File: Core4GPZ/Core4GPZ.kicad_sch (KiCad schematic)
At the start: 5 parts, among them J1 Delphi_Sicma_24, J2 Delphi_Sicma_24, U1 core4, U2 MPX4250

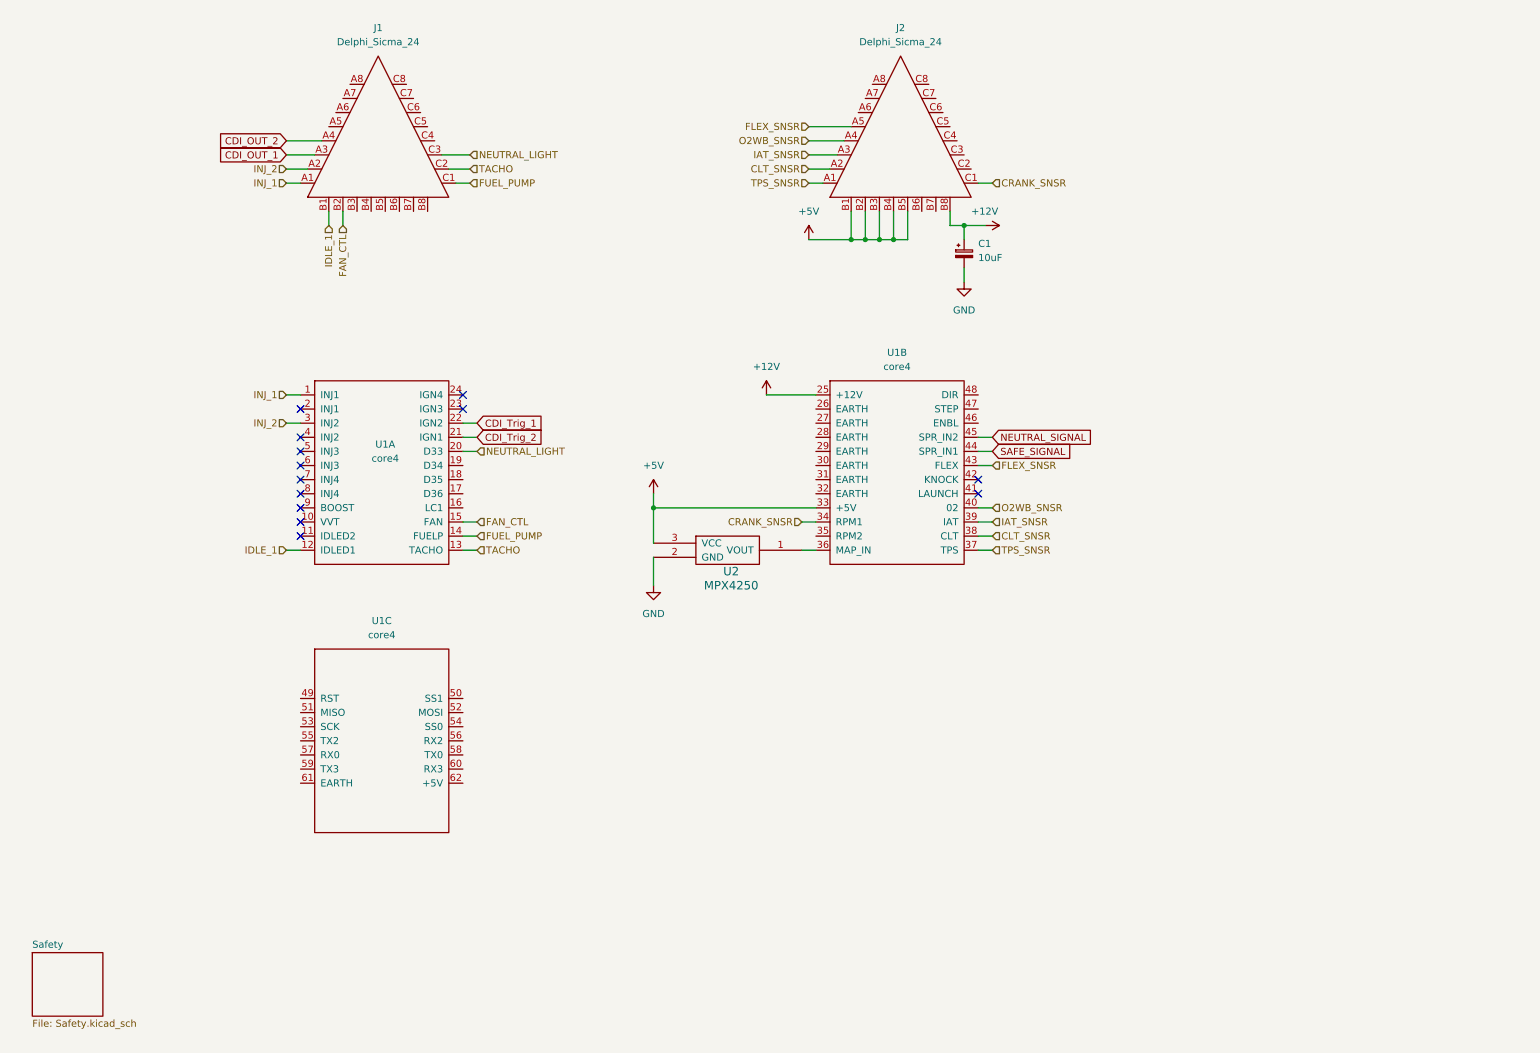
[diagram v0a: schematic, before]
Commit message: Add a splited CDI module. First Design of Ignition coil driver
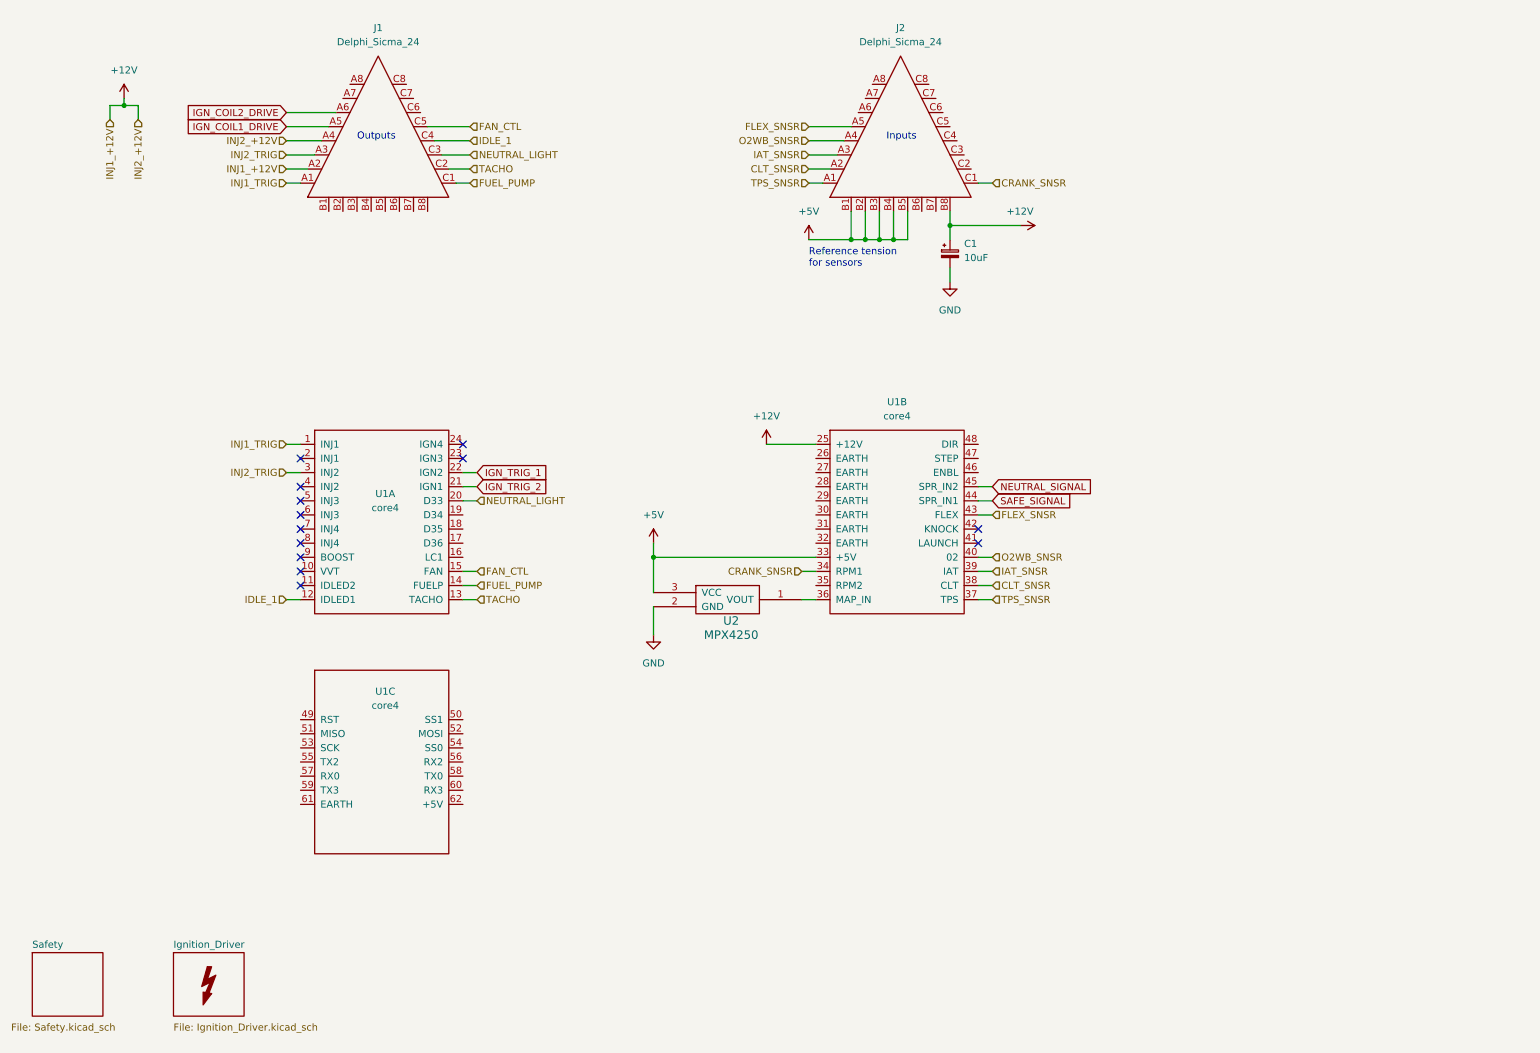
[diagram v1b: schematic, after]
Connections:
- net CDI_OUT_2 is gone; now on net +12V: J1.A4
- net +12V: now also J1.A2
- net FAN_CTL: now also J1.C5; no longer J1.B2
- net IDLE_1: now also J1.C4; no longer J1.B1
- net IGN_COIL1_DRIVE: now reaches J1.A5
- net IGN_COIL2_DRIVE: now reaches J1.A6
- net CDI_OUT_1 renamed INJ2_TRIG
- net INJ2_TRIG: now also U1.3 (INJ2)
- net CDI_Trig_1 renamed IGN_TRIG_1
- net CDI_Trig_2 renamed IGN_TRIG_2
- net INJ_1 renamed INJ1_TRIG
- removed net INJ_2: J1.A2, U1.3 (INJ2)
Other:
- added sheet Ignition_Driver (Ignition_Driver.kicad_sch)
- note added: "Inputs"
- note added: "Outputs"
- note added: "Reference tension for sensors"
- moved on the sheet: C1, U1A, U1B, U1C, U2

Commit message: Updated security wiring and changed IGN driver for MOSFET
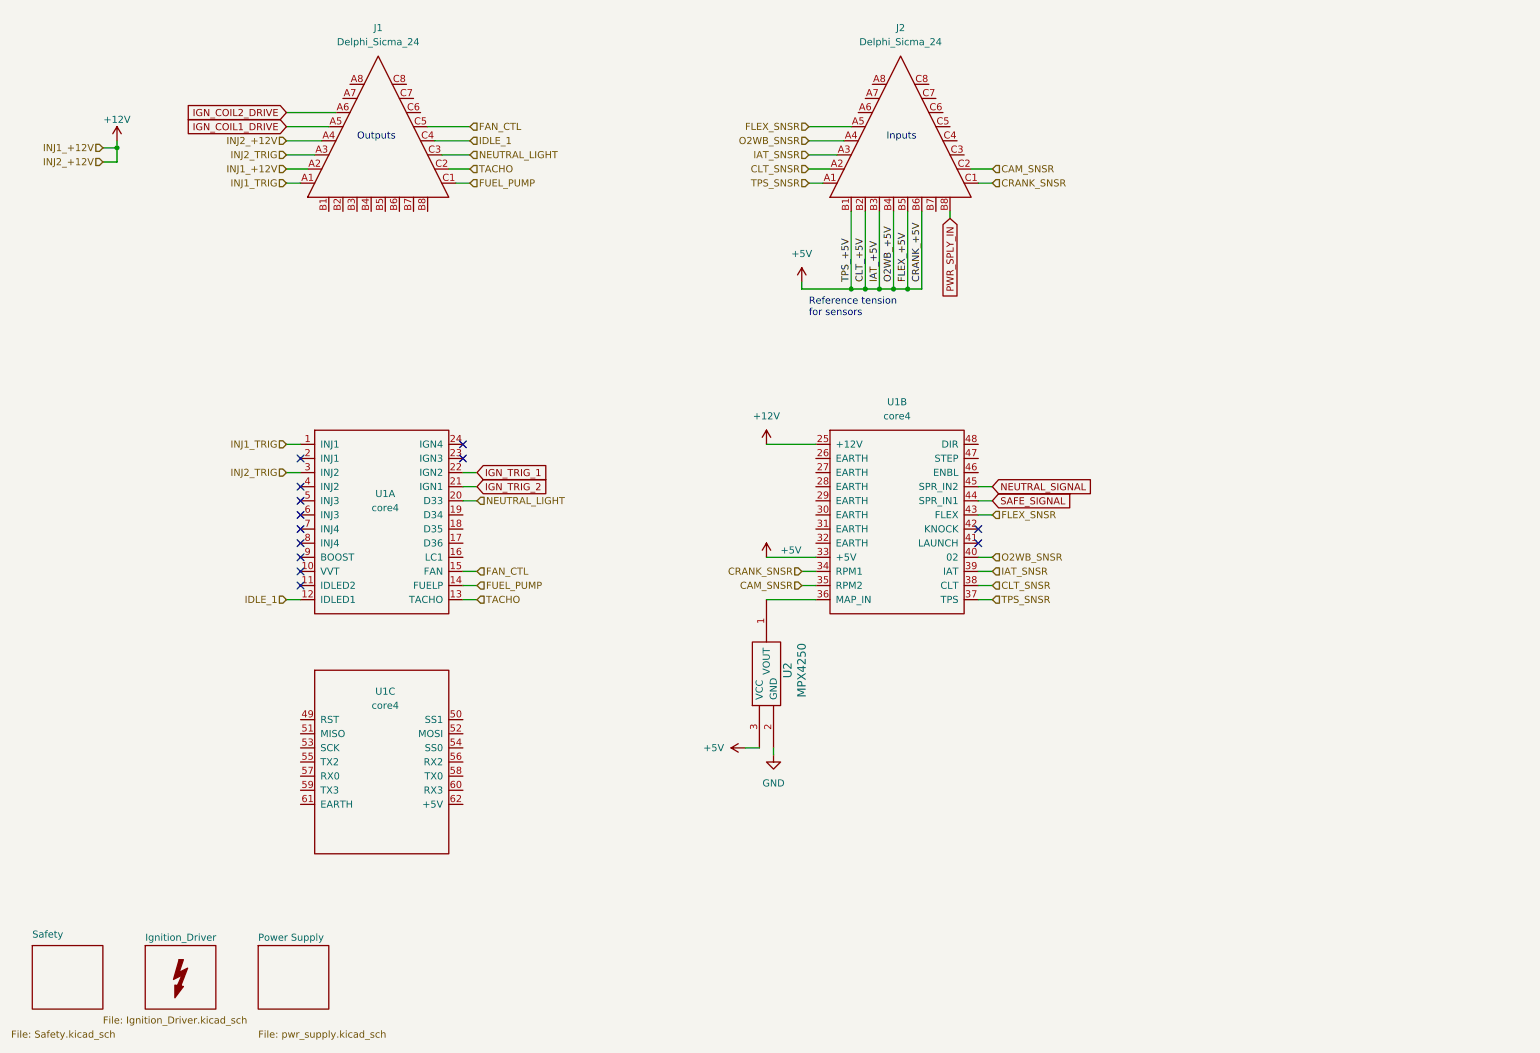
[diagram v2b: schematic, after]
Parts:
- removed C1: 10uF, symbol Device:C_Polarized_Small
- J1: footprint Connector_Automotive:Delphi_Sicma_24_Black -> Speeduino_Conn_Automotive:Delphi_Sicma_24_Black
- J2: footprint Connector_Automotive:Delphi_Sicma_24_Black -> Speeduino_Conn_Automotive:Delphi_Sicma_24_Grey
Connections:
- net +12V: no longer J2.B8
- net +5V: now also J2.B6
- net CAM_SNSR: now reaches U1.35 (RPM2)
- net CAM_SNSR: now also J2.C2
- new net PWR_SPLY_IN: J2.B8
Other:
- added sheet Power Supply (pwr_supply.kicad_sch)
- moved on the sheet: U2

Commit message: Changed Connectors for Molex CMC 48pins Black.
Changed ECU Connector for Molex CMC 48pins Black, for compacity and cost reduction. Designed custom Footprint for this purpose
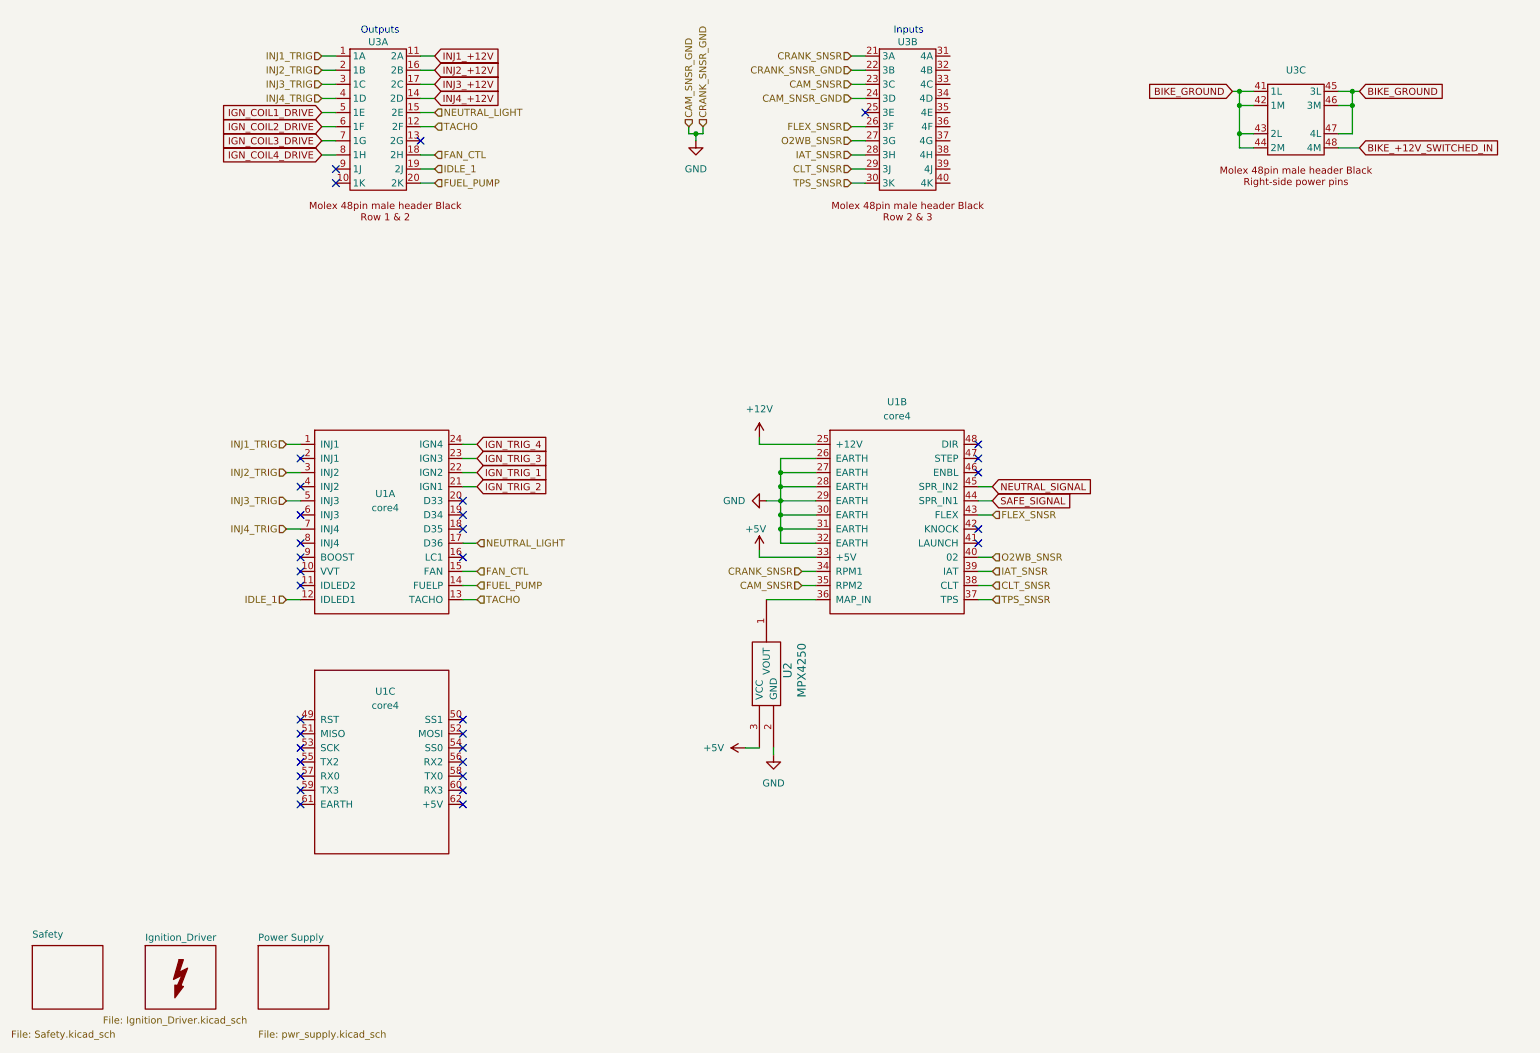
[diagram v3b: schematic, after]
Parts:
- removed J1: Delphi_Sicma_24, Speeduino_Conn_Automotive:Delphi_Sicma_24_Black, symbol Speeduino_Connector_Automotive:Delphi_Sicma_24
- removed J2: Delphi_Sicma_24, Speeduino_Conn_Automotive:Delphi_Sicma_24_Grey, symbol Speeduino_Connector_Automotive:Delphi_Sicma_24
- added U3: ~, Molex_CMC_Conn:Molex_CMC_48pin_Male_Black, symbol Molex_CMC_Conn:Molex_Conn_48_Male_Black
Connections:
- net CAM_SNSR: now also U3.23 (3C)
- net CLT_SNSR: now also U3.29 (3J)
- net CRANK_SNSR: now also U3.21 (3A)
- net FAN_CTL: now also U3.18 (2H)
- net FLEX_SNSR: now also U3.26 (3F)
- net FUEL_PUMP: now also U3.20 (2K)
- net GND: now also U1.26 (EARTH), U1.27 (EARTH), U1.28 (EARTH), U1.29 (EARTH), U1.30 (EARTH), U1.31 (EARTH), U1.32 (EARTH), U3.22 (3B), U3.24 (3D)
- net IAT_SNSR: now also U3.28 (3H)
- net IDLE_1: now also U3.19 (2J)
- net IGN_COIL1_DRIVE: now also U3.5 (1E)
- net IGN_COIL2_DRIVE: now also U3.6 (1F)
- net INJ1_TRIG: now also U3.1 (1A)
- net INJ2_TRIG: now also U3.2 (1B)
- net NEUTRAL_LIGHT: now also U1.17 (D36), U3.15 (2E); no longer U1.20 (D33)
- net O2WB_SNSR: now also U3.27 (3G)
- net TACHO: now also U3.12 (2F)
- net TPS_SNSR: now also U3.30 (3K)
- net IGN_TRIG_3: now reaches U1.23 (IGN3)
- net IGN_TRIG_4: now reaches U1.24 (IGN4)
- net INJ3_TRIG: now reaches U1.5 (INJ3)
- net INJ3_TRIG: now also U3.3 (1C)
- net INJ4_TRIG: now reaches U1.7 (INJ4)
- net INJ4_TRIG: now also U3.4 (1D)
- new net BIKE_+12V_SWITCHED_IN: U3.48 (4M)
- new net BIKE_GROUND: U3.41 (1L), U3.42 (1M), U3.43 (2L), U3.44 (2M), U3.45 (3L), U3.46 (3M), U3.47 (4L)
- new net IGN_COIL3_DRIVE: U3.7 (1G)
- new net IGN_COIL4_DRIVE: U3.8 (1H)
- new net INJ1_+12V: U3.11 (2A)
- new net INJ2_+12V: U3.16 (2B)
- new net INJ3_+12V: U3.17 (2C)
- new net INJ4_+12V: U3.14 (2D)
- no-connect marks 13 -> 34
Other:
- note removed: "Reference tension for sensors"

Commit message: Test montage générateur de Haute tension
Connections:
- net BIKE_+12V_SWITCHED_IN: now also U3.41 (1L); no longer U3.48 (4M)
- net BIKE_GROUND: now also U3.48 (4M); no longer U3.41 (1L)
- net CAM_SNSR: now also U3.22 (3B); no longer U3.23 (3C)
- net GND: no longer U3.22 (3B), U3.24 (3D)
- net IGN_TRIG_1: now also U1.21 (IGN1); no longer U1.22 (IGN2)
- net IGN_TRIG_2: now also U1.22 (IGN2); no longer U1.21 (IGN1)
- net SideStand_SWITCH: now reaches U3.31 (4A)
- net Neutral_SWITCH: now reaches U3.32 (4B)
- net Clutch_SWITCH: now reaches U3.33 (4C)
- net SPR1_SWITCH: now reaches U3.34 (4D)
- net SPR1_SWITCH: now also U3.35 (4E)
- net FLEX_+5V: now reaches U3.36 (4F)
- net O2WB_+5V: now reaches U3.37 (4G)
- net IAT_+5V: now reaches U3.38 (4H)
- net CLT_+5V: now reaches U3.39 (4J)
- net TPS_+5V: now reaches U3.40 (4K)
- net O2WB_SNSR renamed 02_SNSR
- net 02_SNSR: no longer U1.40 (02)
- new net O2_SNSR: U1.40 (02)
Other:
- moved on the sheet: U1A, U1B, U1C, U2, U3A, U3B, U3C

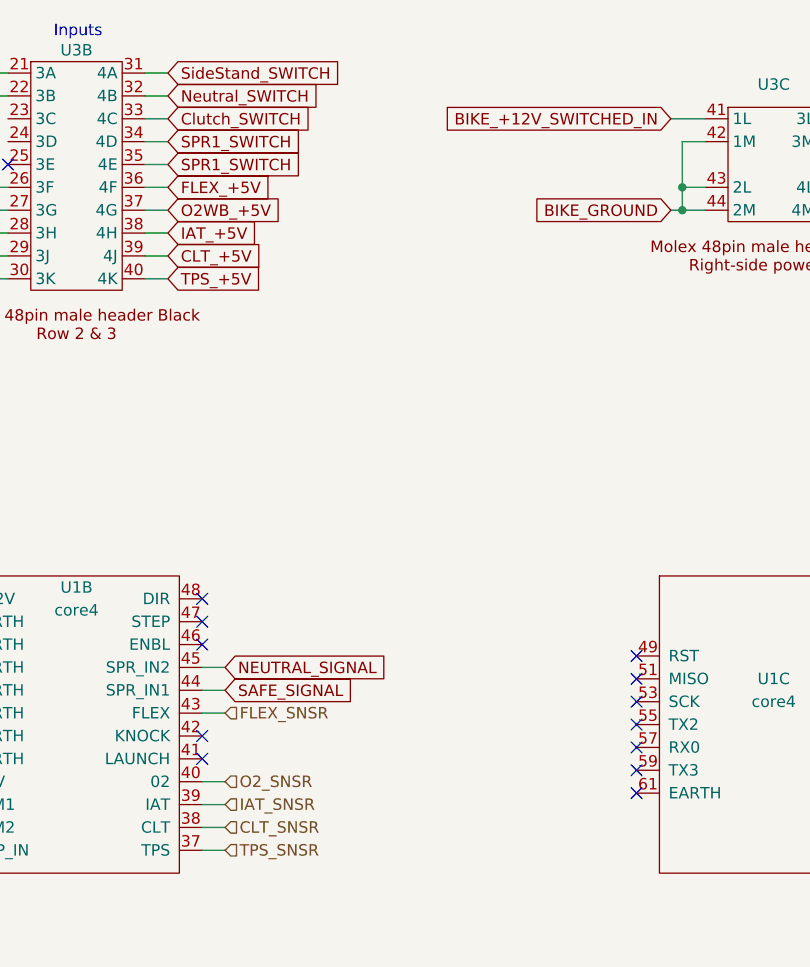
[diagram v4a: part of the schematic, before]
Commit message: Updated to Kicad 8.0
Also added Highvoltage circuit
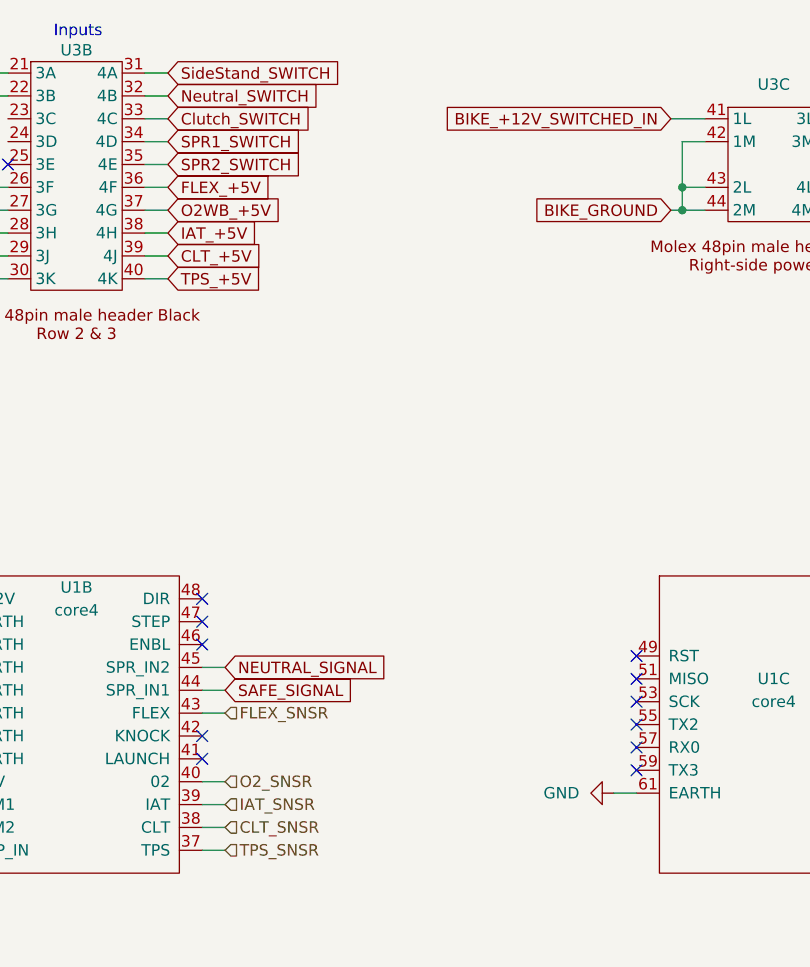
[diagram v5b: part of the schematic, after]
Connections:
- net GND: now also U1.61 (EARTH)
- net SPR1_SWITCH: no longer U3.35 (4E)
- new net SPR2_SWITCH: U3.35 (4E)
- no-connect marks 34 -> 33
